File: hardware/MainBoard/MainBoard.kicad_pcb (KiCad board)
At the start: 2 copper layers, 50 x 80 mm, 31 parts, among them J101 Servo, J102 Relay, J103 MotorDriver, J104 MPU9250, J105 PicoBATT+, J106 Tachometer, J201 Micro_SD_Card, SW101 Reset, SW102 SW_Pico, SW103 SW_BATT

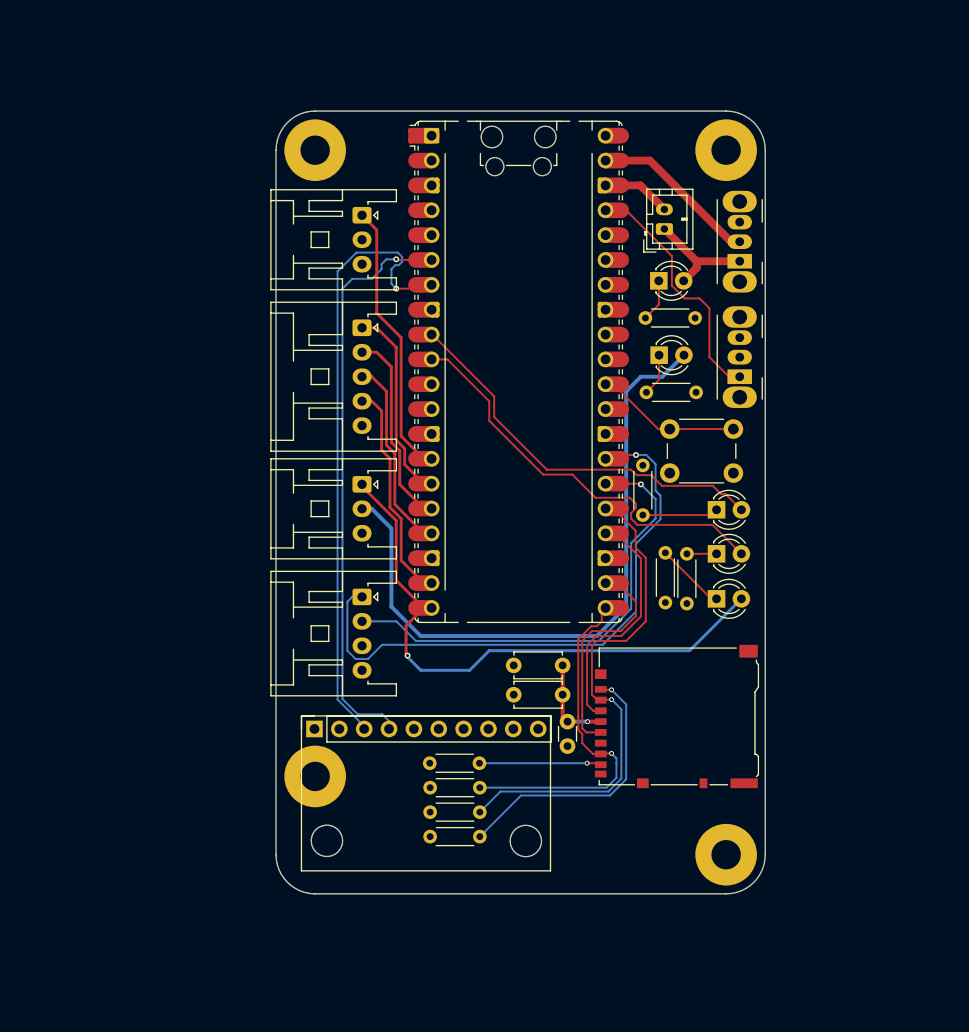
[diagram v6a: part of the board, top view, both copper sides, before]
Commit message: 追加し忘れ（未配線0）
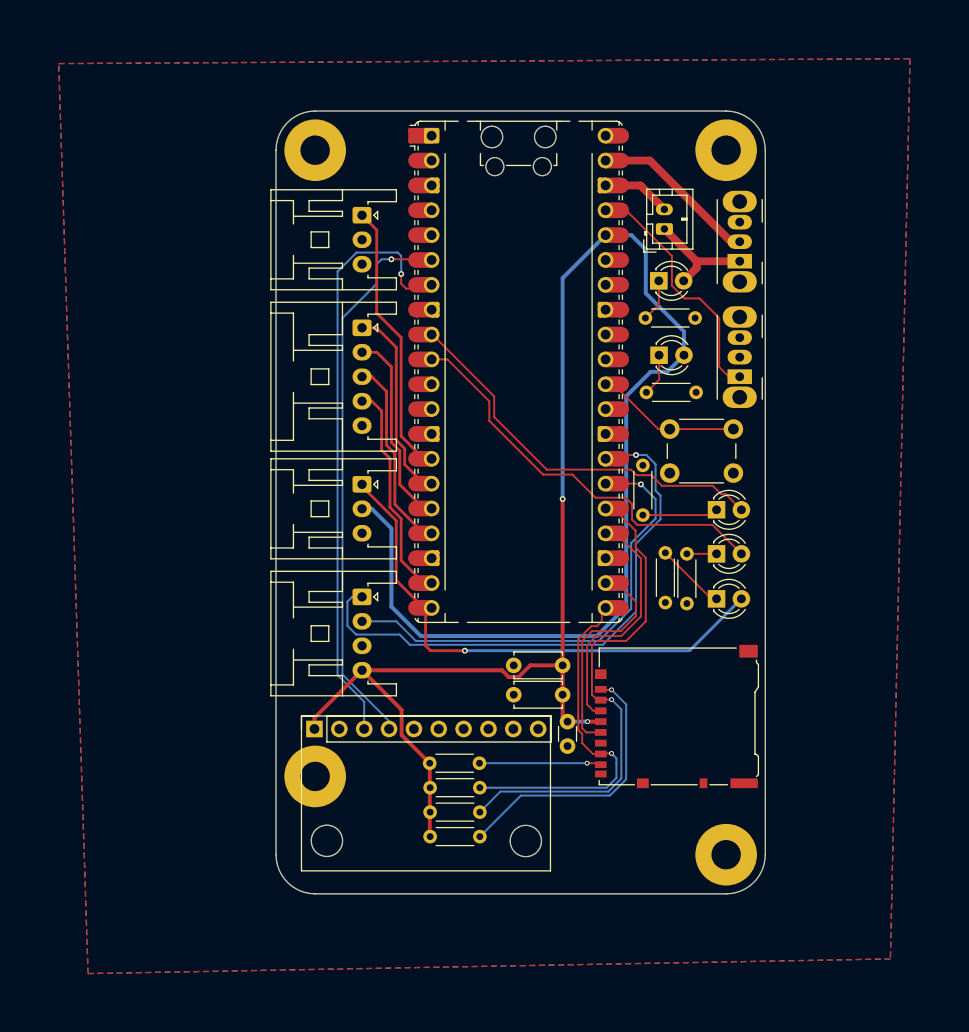
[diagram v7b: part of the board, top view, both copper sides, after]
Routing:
- net VDD: track 77.1 -> 188.9 mm, vias 1 -> 2
- net /Relay_S: track 58.8 -> 53.9 mm
- net /OUT2: track 59.7 -> 57.0 mm
- net /SDA: track 58.3 -> 56.0 mm
- net /SCL: track 62.6 -> 60.9 mm
- net /ERROR: track 42.6 -> 42.0 mm
- added copper zone on B.Cu, net GND
- added copper zone on F.Cu, net GND

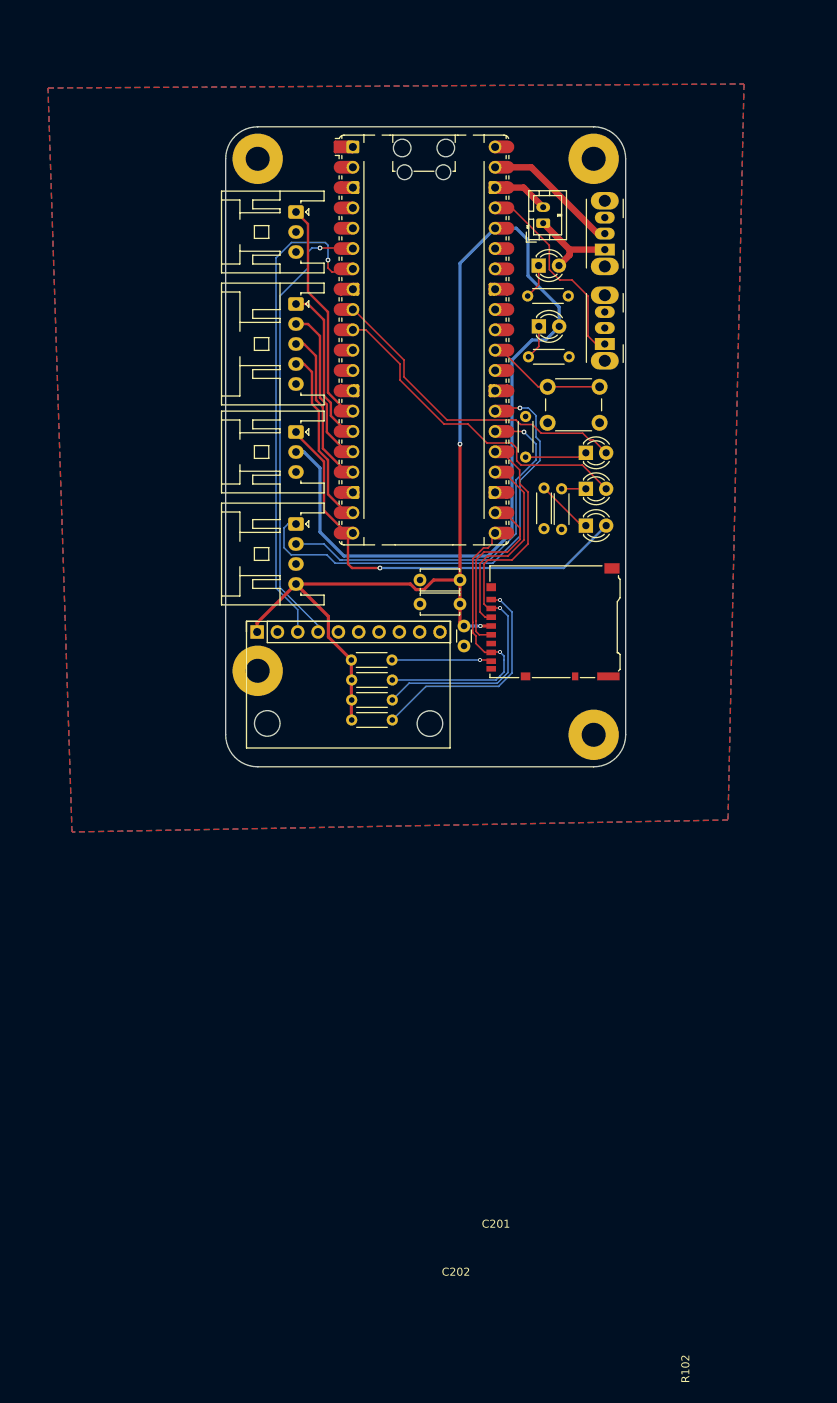
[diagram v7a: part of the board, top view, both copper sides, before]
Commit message: 配線をいくつか太くした。もう少し太くできるかも。
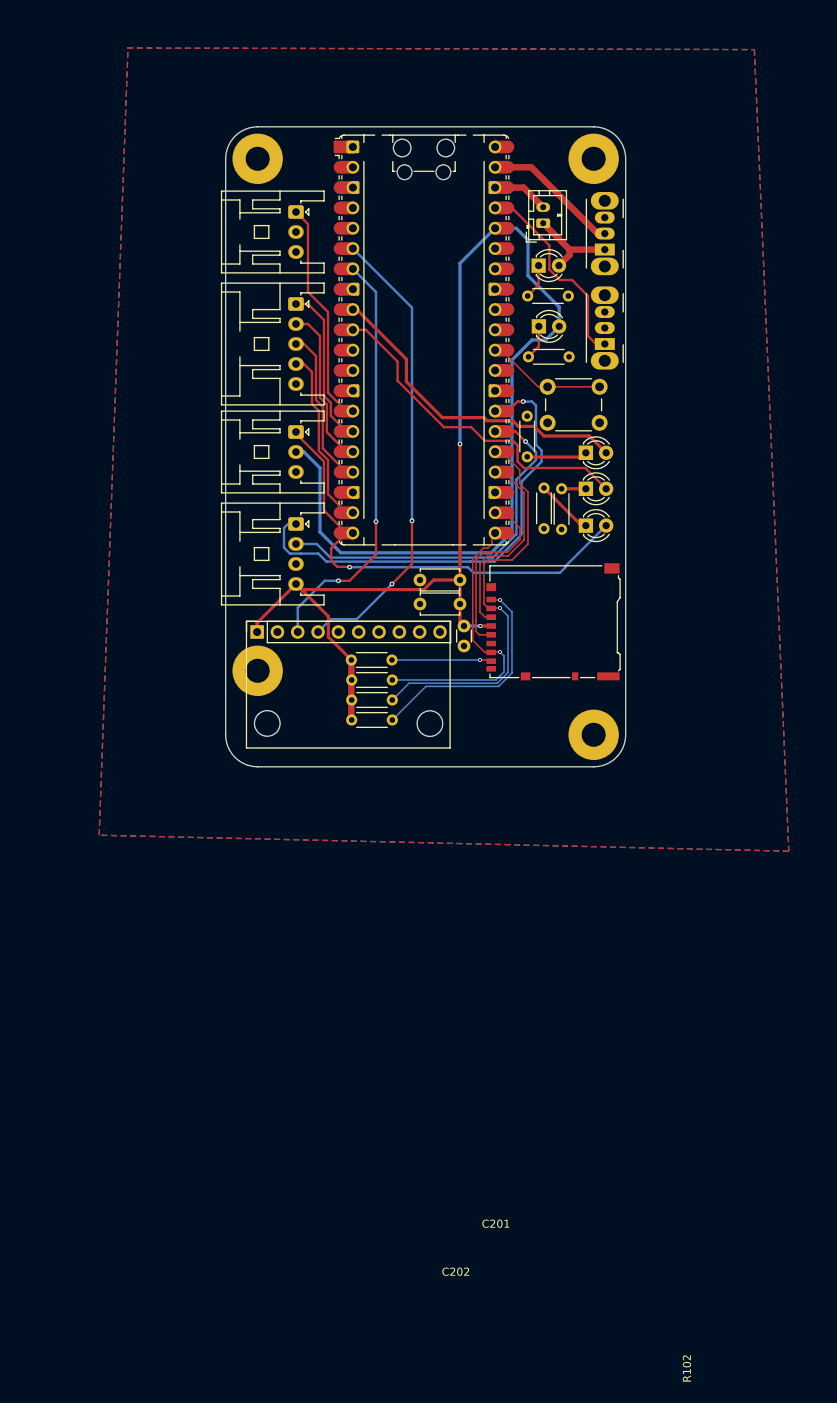
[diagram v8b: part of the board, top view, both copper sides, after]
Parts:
- moved R102 0.20 mm to (152.9, 72.5)
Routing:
- net /SCL: track 60.9 -> 52.5 mm, vias 1 -> 2
- net /Relay_S: track 53.9 -> 57.0 mm
- net /SDA: track 56.0 -> 57.9 mm, vias 1 -> 2
- net /OUT2: track 57.0 -> 58.4 mm
- net /OUT1: track 46.9 -> 46.1 mm
- net /ERROR: track 42.0 -> 42.5 mm
